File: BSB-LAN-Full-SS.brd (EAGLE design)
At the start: 86.5 x 49.4 mm, 122 parts, among them IC1 LAN8710A-EZC, IC2 TPS2375D, IC3 TX4138, IC4 SY8089AAAC, IC6 CH340X, Q1 BC847, Q2 BC857, Q3 BC847, Q4 WPM2015-3/TR, Q5 BC847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

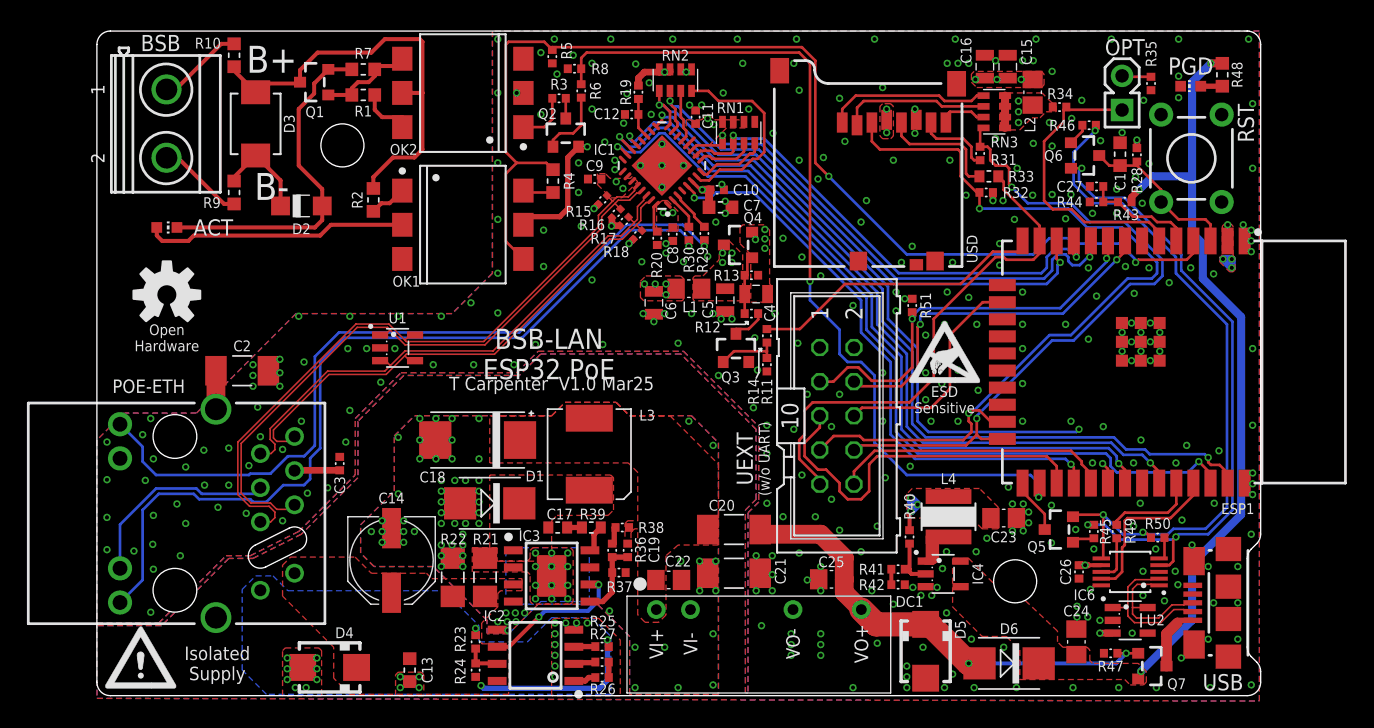
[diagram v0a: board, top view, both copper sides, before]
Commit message: Fix RJ45 Position on Full-SS Board
To ensure it's pins don't foul the PCB keepout zone.
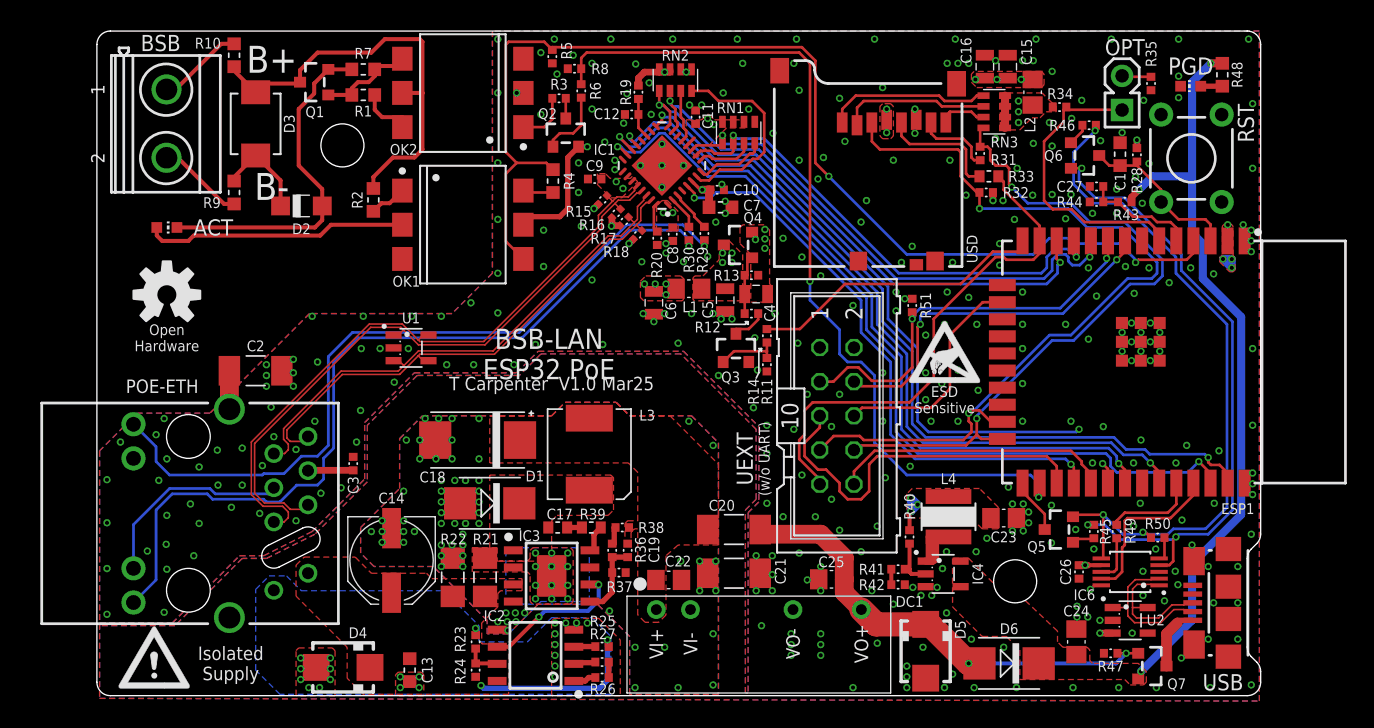
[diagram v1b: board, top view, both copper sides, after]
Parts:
- moved C2 1.00 mm to (11.8, 24.4)
- moved C3 1.00 mm to (19.1, 17.4)
- moved D4 1.00 mm to (18.3, 2.30)
- moved POE-ETH 1.00 mm to (6.80, 13.8)
- moved U$1 1.00 mm to (4.25, 2.50)
- moved U1 1.00 mm to (23.4, 26.1)
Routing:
- net ETH-VDDA: track 62.7 -> 61.7 mm
- net ETH-TD_P: track 48.9 -> 47.9 mm
- net ETH-TD_N: track 49.6 -> 48.6 mm
- net ETH-RD_P: track 39.6 -> 38.6 mm
- net ETH-RD_N: track 40.2 -> 39.2 mm
- net ETH-LED1-A: track 58.3 -> 57.3 mm
- net ETH-LED-G-K: track 63.2 -> 62.2 mm

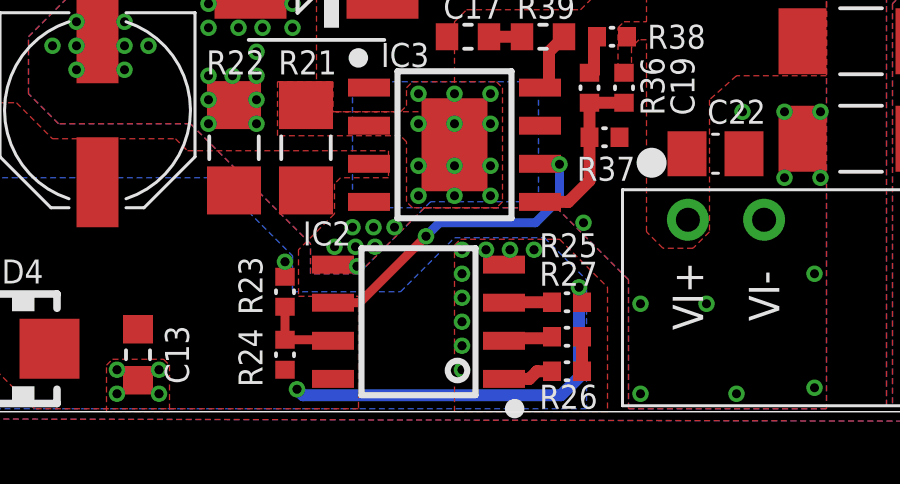
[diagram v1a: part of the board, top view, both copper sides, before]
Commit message: Correct PoE IC Part Number
The LCSC_PART selected was the TPS2376DDA but the schematic value was TPS2375D, This actually has a slightly different footprint - the DDA has a thermal pad.

Update to account for the change.
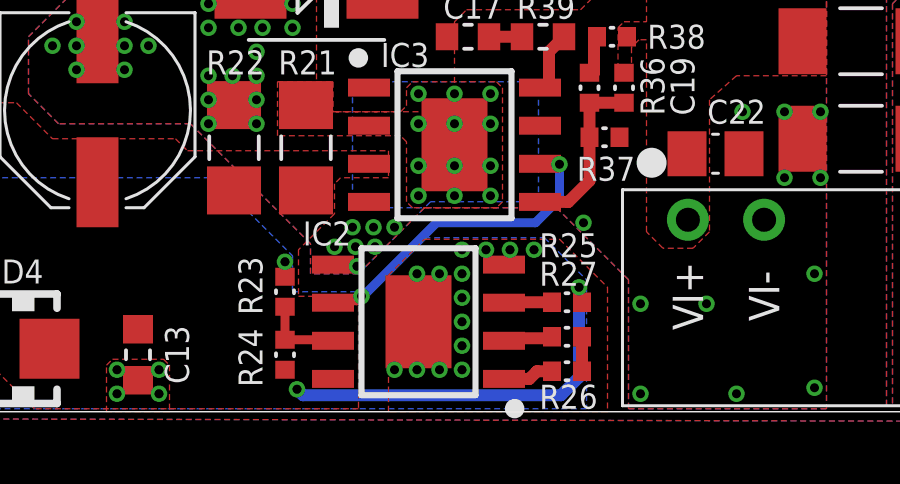
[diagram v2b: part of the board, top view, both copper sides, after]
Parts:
- IC2: value TPS2375D -> TPS2376DDA; device BSB-LAN:SOIC8 -> BSB-LAN:SOIC8-EP
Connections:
- net POE-V-: now also IC2.EP
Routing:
- net POE-V-: vias 22 -> 27
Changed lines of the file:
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@@
 <attribute name="LCSC_PART" value="C113803" x="23.25" y="2.1" size="1.778" layer="27" rot="R270" display="off"/>
 </element>
-<element name="IC2" library="BSB-LAN" package="SOIC8" value="TPS2375D" x="32.6" y="3.2" smashed="yes" rot="R90">
+<element name="IC2" library="BSB-LAN" package="SOIC8-EP" value="TPS2376DDA" x="32.6" y="3.2" smashed="yes" rot="R90">
 <attribute name="LCSC_PART" value="C544899" x="32.6" y="3.2" size="1" layer="27" font="vector" ratio="15" rot="R90" display="off"/>
 <attribute name="NAME" x="29.55" y="6.1425" size="0.8" layer="25" font="vector" ratio="15" align="center"/>
@@
 <vertex x="28.4" y="5.4"/>
 <vertex x="28.4" y="4.2"/>
-<vertex x="32" y="4.2"/>
-<vertex x="33.8" y="6"/>
+<vertex x="31" y="4.2"/>
+<vertex x="32.8" y="6"/>
 <vertex x="36.8" y="6"/>
 <vertex x="38.2" y="4.6"/>
@@
 </polygon>
 <polygon width="0.2" layer="1" spacing="0.2" isolate="0.2" thermals="no">
-<vertex x="33.8" y="0.2"/>
-<vertex x="33.8" y="5.75"/>
-<vertex x="34" y="5.95"/>
+<vertex x="38.9" y="0.2"/>
+<vertex x="31.6" y="0.2"/>
+<vertex x="31.6" y="4.75"/>
+<vertex x="32.8" y="5.95"/>
 <vertex x="37.3" y="5.95"/>
 <vertex x="38.9" y="4.35"/>
-<vertex x="38.9" y="0.2"/>
 </polygon>
 <via x="34.05" y="4.8" extent="1-16" drill="0.3"/>
@@
 <via x="15.75" y="0.8" extent="1-16" drill="0.3"/>
 <via x="16.55" y="0.8" extent="1-16" drill="0.3"/>
+<contactref element="IC2" pad="EP"/>
+<via x="32.55" y="1.6" extent="1-16" drill="0.3"/>
+<via x="33.3" y="1.6" extent="1-16" drill="0.3"/>
+<via x="32.55" y="4.8" extent="1-16" drill="0.3"/>
+<via x="33.3" y="4.8" extent="1-16" drill="0.3"/>
+<via x="31.8" y="1.6" extent="1-16" drill="0.3"/>
 </signal>
 <signal name="POE-V+" class="2">
@@
 <wire x1="37.3" y1="8.45" x2="36.65" y2="8.45" width="0.4" layer="1"/>
 <wire x1="36.65" y1="8.45" x2="36.65" y2="8.465" width="0.4" layer="1"/>
-<wire x1="32.85" y1="6.05" x2="33.3" y2="6.5" width="0.3" layer="16"/>
-<wire x1="33.3" y1="6.5" x2="36.5" y2="6.5" width="0.3" layer="16"/>
+<wire x1="30.7" y1="4.05" x2="30.75" y2="4.05" width="0.3" layer="16"/>
+<wire x1="30.75" y1="4.05" x2="33.2" y2="6.5" width="0.3" layer="16"/>
+<wire x1="33.2" y1="6.5" x2="36.5" y2="6.5" width="0.3" layer="16"/>
 <wire x1="36.5" y1="6.5" x2="37.3" y2="7.3" width="0.3" layer="16"/>
 <wire x1="37.3" y1="7.3" x2="37.3" y2="8.45" width="0.3" layer="16"/>
-<wire x1="29.75" y1="3.835" x2="30.635" y2="3.835" width="0.3" layer="1"/>
-<wire x1="30.635" y1="3.835" x2="32.85" y2="6.05" width="0.3" layer="1"/>
-<via x="32.85" y="6.05" extent="1-16" drill="0.3"/>
+<wire x1="29.75" y1="3.835" x2="29.75" y2="3.9" width="0.3" layer="1"/>
+<wire x1="29.75" y1="3.9" x2="30.55" y2="3.9" width="0.3" layer="1"/>
+<wire x1="30.55" y1="3.9" x2="30.7" y2="4.05" width="0.3" layer="1"/>
+<via x="30.7" y="4.05" extent="1-16" drill="0.3"/>
 </signal>
 <signal name="POE-UVLO" class="2">

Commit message: Correct Component Rotation Values in JLC CPL
Add rotation correction factors to parts which import in the wrong orientation.
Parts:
- UEXT: value DNI -> 2x5 IDC
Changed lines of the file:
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@@
 <layer number="220" name="220bmp" color="21" fill="1" visible="no" active="no"/>
 <layer number="221" name="221bmp" color="22" fill="1" visible="no" active="no"/>
+<layer number="222" name="222bmp" color="7" fill="1" visible="yes" active="yes"/>
 <layer number="223" name="223bmp" color="24" fill="1" visible="no" active="no"/>
 <layer number="224" name="224bmp" color="25" fill="1" visible="no" active="no"/>
@@
 <attribute name="LCSC_PART" value="C130417" x="50.49" y="87.71" size="1.778" layer="27" rot="R90" display="off"/>
 <attribute name="NAME" x="16.2" y="43.6" size="0.8" layer="25" font="vector" ratio="15" align="center"/>
+<attribute name="JLC_ROT" value="270" x="16.2" y="45.8" size="1.778" layer="27" rot="R90" display="off"/>
 </element>
 <element name="Q2" library="BSB-LAN" package="SOT23-BEC" value="BC857" x="34.85" y="42" smashed="yes">
 <attribute name="LCSC_PART" value="C426782" x="50.09" y="2.63" size="1.778" layer="27" display="off"/>
 <attribute name="NAME" x="33.4945" y="43.463" size="0.8" layer="25" font="vector" ratio="15" align="center"/>
-</element>
-<element name="UEXT" library="BSB-LAN" package="ML10" value="DNI" x="55" y="21" smashed="yes" rot="R270">
+<attribute name="JLC_ROT" value="270" x="34.85" y="42" size="1.778" layer="27" display="off"/>
+</element>
+<element name="UEXT" library="BSB-LAN" package="ML10" value="2x5 IDC" x="55" y="21" smashed="yes" rot="R270">
 <attribute name="NAME" x="48.15" y="17.8" size="1.2" layer="25" font="vector" ratio="15" rot="R270" align="center"/>
 <attribute name="VALUE" x="49.92" y="21" size="1.778" layer="27" font="vector" ratio="15" rot="R270" align="center"/>
+<attribute name="LCSC_PART" value="C5665" x="55" y="21" size="1.778" layer="27" rot="R270" display="off"/>
 </element>
 <element name="ACT" library="BSB-LAN" package="CHIP-LED0603" value="red" x="5.2" y="35" smashed="yes" rot="R270">
@@
 <attribute name="NAME" x="8.65" y="35.005" size="1.2" layer="25" font="vector" ratio="15" align="center"/>
 <attribute name="VALUE" x="5.2" y="33.095" size="1.27" layer="27" font="vector" ratio="15" align="center"/>
+<attribute name="JLC_ROT" value="270" x="5.2" y="35" size="1.778" layer="27" rot="R270" display="off"/>
 </element>
 <element name="R3" library="BSB-LAN" package="R0402" value="220R" x="34.35" y="44.6" smashed="yes" rot="R180">
@@
 <attribute name="NAME" x="37.7292875" y="40.8" size="0.8" layer="25" font="vector" ratio="15" align="center"/>
 <attribute name="VALUE" x="44.474871875" y="42.074875" size="0.8" layer="27" font="vector" ratio="15" rot="R135" align="center"/>
+<attribute name="JLC_ROT" value="270" x="42" y="39.6" size="1.778" layer="27" rot="R135" display="off"/>
 </element>
 <element name="POE-ETH" library="BSB-LAN" package="HY931147C-SLOT" value="HY931147C-SLOT" x="6.8" y="13.75" smashed="yes" rot="R90">
@@
 <attribute name="NAME" x="4.85" y="23.2" size="1" layer="25" font="vector" ratio="15" align="center"/>
 <attribute name="VALUE" x="10.3" y="13.75" size="1" layer="27" font="vector" ratio="15" rot="R270" align="center"/>
+<attribute name="JLC_ROT" value="270" x="6.8" y="13.75" size="1.778" layer="27" rot="R90" display="off"/>
 </element>
 <element name="Q3" library="BSB-LAN" package="SOT23" value="BC847" x="47.5" y="26" smashed="yes">
 <attribute name="LCSC_PART" value="C130417" x="47.5" y="26" size="1" layer="27" font="vector" ratio="15" display="off"/>
 <attribute name="NAME" x="47.1055" y="23.887" size="0.8" layer="25" font="vector" ratio="15" rot="R180" align="center"/>
+<attribute name="JLC_ROT" value="270" x="47.5" y="26" size="1.778" layer="27" display="off"/>
 </element>
 <element name="Q4" library="BSB-LAN" package="SOT23" value="WPM2015-3/TR" x="47.7" y="33.7" smashed="yes" rot="R90">
 <attribute name="LCSC_PART" value="C7472861" x="47.7" y="33.7" size="1" layer="27" font="vector" ratio="15" rot="R90" display="off"/>
 <attribute name="NAME" x="48.7555" y="35.737" size="0.8" layer="25" font="vector" ratio="15" rot="R180" align="center"/>
+<attribute name="JLC_ROT" value="270" x="47.7" y="33.7" size="1.778" layer="27" rot="R90" display="off"/>
 </element>
 <element name="U1" library="BSB-LAN" package="DBV0005A-SOT23" value="ESDS314DBV" x="23.35" y="26.05" smashed="yes" rot="R270">
@@
 <attribute name="VALUE" x="47.7" y="40.145" size="1.016" layer="27" font="vector" ratio="15" align="center"/>
 <attribute name="LCSC_PART" value="C414564" x="47.7" y="42.05" size="1.778" layer="27" display="off"/>
+<attribute name="JLC_ROT" value="270" x="47.7" y="42.05" size="1.778" layer="27" display="off"/>
 </element>
 <element name="RN2" library="BSB-LAN" package="CTS742C083" value="2.2k" x="43" y="45.95" smashed="yes">
@@
 <attribute name="VALUE" x="43" y="44.045" size="1.016" layer="27" font="vector" ratio="15" align="center"/>
 <attribute name="LCSC_PART" value="C414564" x="43" y="45.95" size="1.778" layer="27" display="off"/>
+<attribute name="JLC_ROT" value="270" x="43" y="45.95" size="1.778" layer="27" display="off"/>
 </element>
 <element name="R13" library="BSB-LAN" package="R0402" value="10k" x="48.65" y="31.45" smashed="yes">
@@
 <attribute name="NAME" x="65.475" y="9.25" size="0.8" layer="25" font="vector" ratio="15" rot="R90" align="center"/>
 <attribute name="VALUE" x="59.725" y="9.25" size="1.27" layer="27" font="vector" ratio="15" rot="R270" align="center"/>
+<attribute name="JLC_ROT" value="270" x="62.9" y="9.25" size="1.778" layer="27" rot="R270" display="off"/>
 </element>
 <element name="ESP1" library="BSB-LAN" package="ESP32-WROOM-32E" value="ESP32-WROOM-32E" x="68.8" y="25" smashed="yes" rot="R270">
@@
 <attribute name="VALUE" x="84.8" y="25" size="0.8" layer="27" font="vector" ratio="15" rot="R270" align="center"/>
 <attribute name="NAME" x="84.8" y="14.1" size="0.8" layer="25" font="vector" ratio="15" align="center"/>
+<attribute name="JLC_ROT" value="270" x="68.8" y="25" size="1.778" layer="27" rot="R270" display="off"/>
 </element>
 <element name="USD" library="BSB-LAN" package="MICRO-SD" value="XKTF-001A" x="50.05" y="47.6" smashed="yes">
@@
 <attribute name="VALUE" x="64.795" y="43.6" size="1.016" layer="27" font="vector" ratio="15" rot="R270" align="center"/>
 <attribute name="LCSC_PART" value="C414564" x="66.7" y="43.6" size="1.778" layer="27" rot="R270" display="off"/>
+<attribute name="JLC_ROT" value="270" x="66.7" y="43.6" size="1.778" layer="27" rot="R270" display="off"/>
 </element>
 <element name="R31" library="BSB-LAN" package="R0402" value="220R" x="65.65" y="40.5" smashed="yes" rot="R270">
@@
 <attribute name="LCSC_PART" value="C130417" x="67.15" y="7.55" size="1.2" layer="27" font="vector" ratio="15" rot="R90" display="off"/>
 <attribute name="NAME" x="69.8555" y="11.287" size="0.8" layer="25" font="vector" ratio="15" rot="R180" align="center"/>
+<attribute name="JLC_ROT" value="270" x="71.55" y="12.55" size="1.778" layer="27" rot="R90" display="off"/>
 </element>
 <element name="R45" library="BSB-LAN" package="R0402" value="1k" x="74.1" y="12.4" smashed="yes" rot="R90">
@@
 <attribute name="LCSC_PART" value="C130417" x="73.4" y="40.35" size="1.2" layer="27" font="vector" ratio="15" rot="R270" display="off"/>
 <attribute name="NAME" x="71.1" y="40.35" size="0.8" layer="25" font="vector" ratio="15" rot="R180" align="center"/>
+<attribute name="JLC_ROT" value="270" x="73.4" y="40.35" size="1.778" layer="27" rot="R270" display="off"/>
 </element>
 <element name="R46" library="BSB-LAN" package="R0402" value="1k" x="73.75" y="42.6" smashed="yes">
@@
 <attribute name="LCSC_PART" value="C7472861" x="82.8" y="7.6" size="1.2" layer="27" font="vector" ratio="15" rot="R270" display="off"/>
 <attribute name="NAME" x="80.2555" y="1.087" size="0.8" layer="25" font="vector" ratio="15" rot="R180" align="center"/>
+<attribute name="JLC_ROT" value="270" x="78.4" y="2.4" size="1.778" layer="27" rot="R270" display="off"/>
 </element>
 <element name="D6" library="BSB-LAN" package="SMB" value="SS510B" x="67.8" y="2.6" smashed="yes" rot="R180">
@@
 <attribute name="NAME" x="81.3" y="47" size="1.27" layer="25" font="vector" ratio="15" rot="R180" align="center"/>
 <attribute name="VALUE" x="81.3" y="47.405" size="1.27" layer="27" font="vector" ratio="15" rot="R180" align="center"/>
+<attribute name="JLC_ROT" value="270" x="81.3" y="45.5" size="1.778" layer="27" rot="R90" display="off"/>
 </element>
 <element name="C26" library="BSB-LAN" package="C0402" value="0.1uF" x="73" y="9.4" smashed="yes" rot="R270">
